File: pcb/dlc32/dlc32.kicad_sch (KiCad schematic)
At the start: 33 parts, among them IC1 74HCT08, IC2 74HCT14, J1 DOOR1, J16 TP, J2 DOOR2, J3 CHILLER_OK, J8 LASER

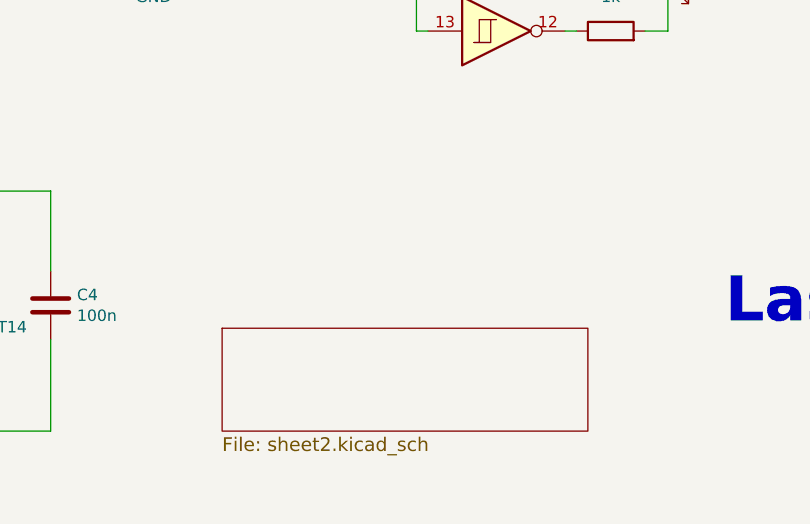
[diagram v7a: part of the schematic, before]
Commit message: Add endstop connectors.
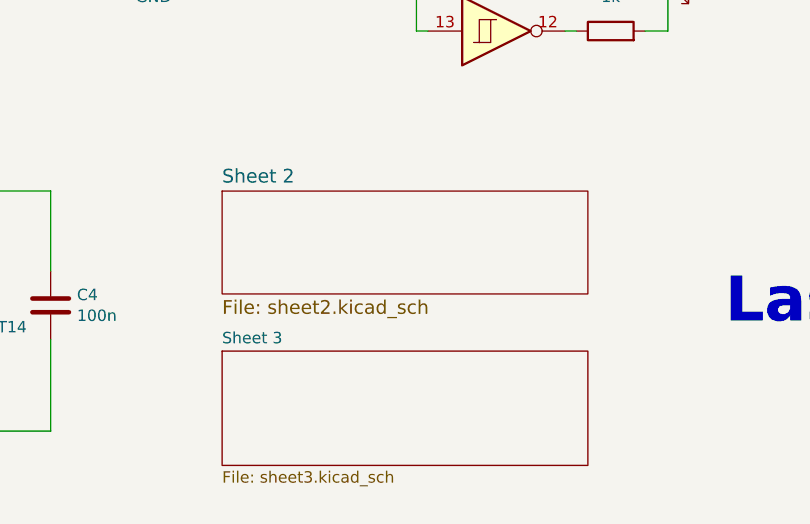
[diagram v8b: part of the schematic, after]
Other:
- sheet Sheet2 renamed Sheet 2
- added sheet Sheet 3 (sheet3.kicad_sch)
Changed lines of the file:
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@@
 	)
 	(sheet
-		(at 124.46 176.53)
+		(at 124.46 161.29)
 		(size 40.64 11.43)
 		(exclude_from_sim no)
@@
 			(color 0 0 0 0.0000)
 		)
-		(property "Sheetname" "Sheet2"
-			(at 124.46 175.7675 0)
+		(property "Sheetname" "Sheet 2"
+			(at 124.46 160.5275 0)
 			(effects
 				(font
@@
 				)
 				(justify left bottom)
-				(hide yes)
 			)
 		)
 		(property "Sheetfile" "sheet2.kicad_sch"
-			(at 124.46 188.5701 0)
+			(at 124.46 173.3301 0)
 			(effects
 				(font
@@
 				)
 			)
+		)
+	)
+	(sheet
+		(at 124.46 179.07)
+		(size 40.64 12.7)
+		(exclude_from_sim no)
+		(in_bom yes)
+		(on_board yes)
+		(dnp no)
+		(fields_autoplaced yes)
+		(stroke
+			(width 0.1524)
+			(type solid)
+		)
+		(fill
+			(color 0 0 0 0.0000)
+		)
+		(property "Sheetname" "Sheet 3"
+			(at 124.46 178.3584 0)
+			(effects
+				(font
+					(size 1.27 1.27)
+				)
+				(justify left bottom)
+			)
+		)
+		(property "Sheetfile" "sheet3.kicad_sch"
+			(at 124.46 192.3546 0)
+			(effects
+				(font
+					(size 1.27 1.27)
+				)
+				(justify left top)
+			)
+		)
+		(instances
+			(project "dlc32"
+				(path "/fc0b2ef6-7d8e-4322-8468-8fac0c3c3d07"
+					(page "3")
+				)
+			)
